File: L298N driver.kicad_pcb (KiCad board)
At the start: 2 copper layers, 75 x 75 mm, 39 parts, among them J1 Screw_Terminal_01x03, J2 Conn_01x02_Pin, J3 Conn_01x05, J4 Conn_01x05, J5 Conn_01x02, J6 Conn_01x02, J7 Conn_01x02, J8 Conn_01x02, U1 74HC595, U2 LM78M05_TO220, U3 DEV-15795, U4 L298N, U5 L298N

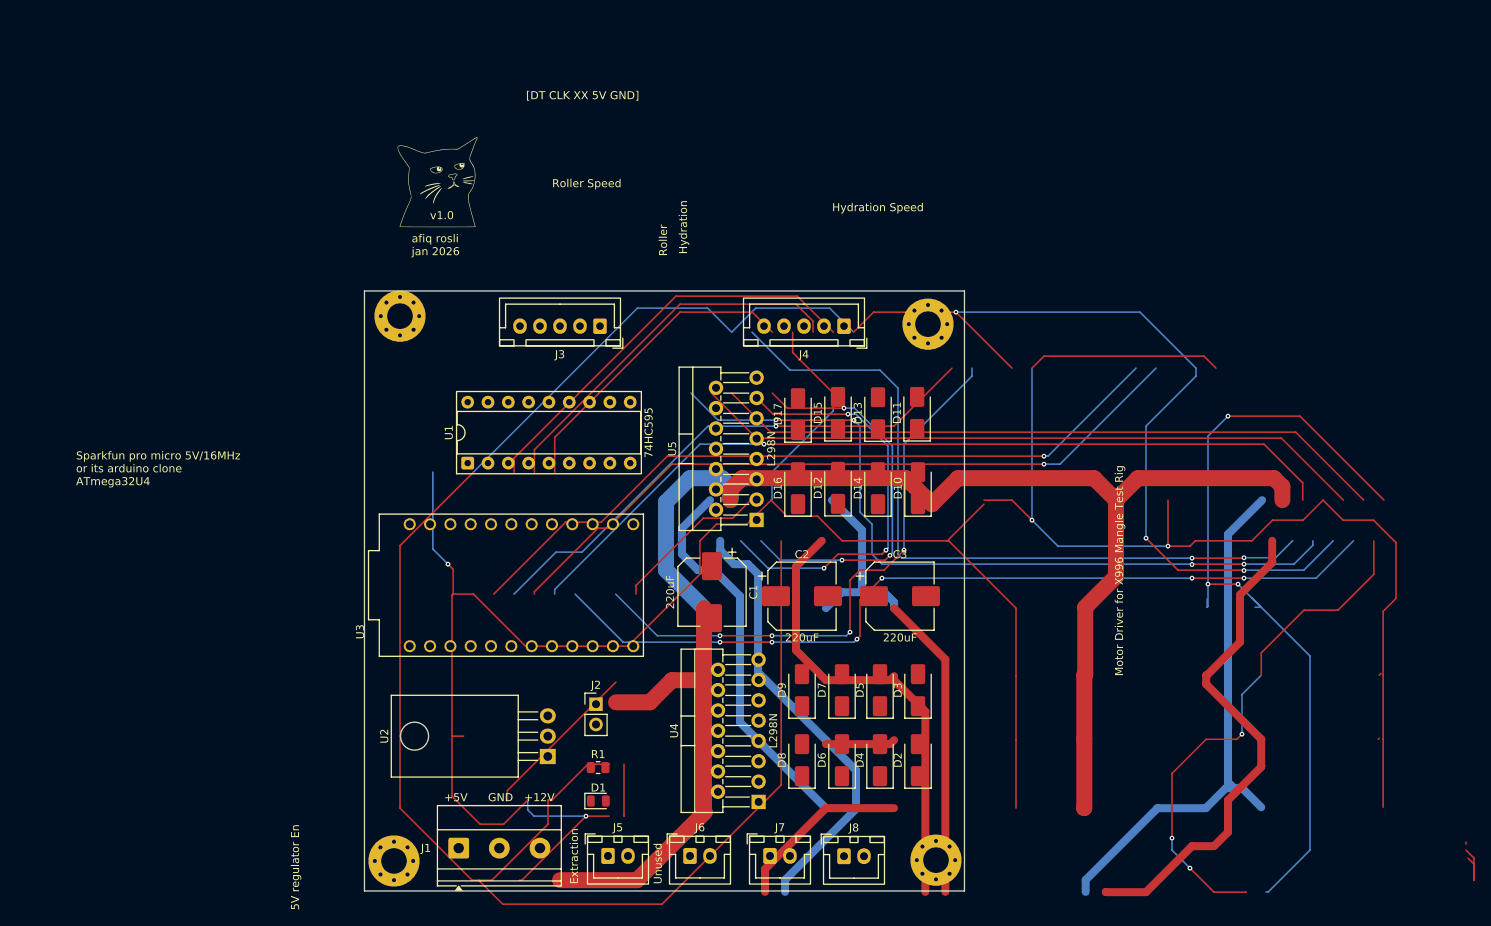
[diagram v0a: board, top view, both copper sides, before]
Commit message: draft layout for smd and 3x3 board. drc error still exist
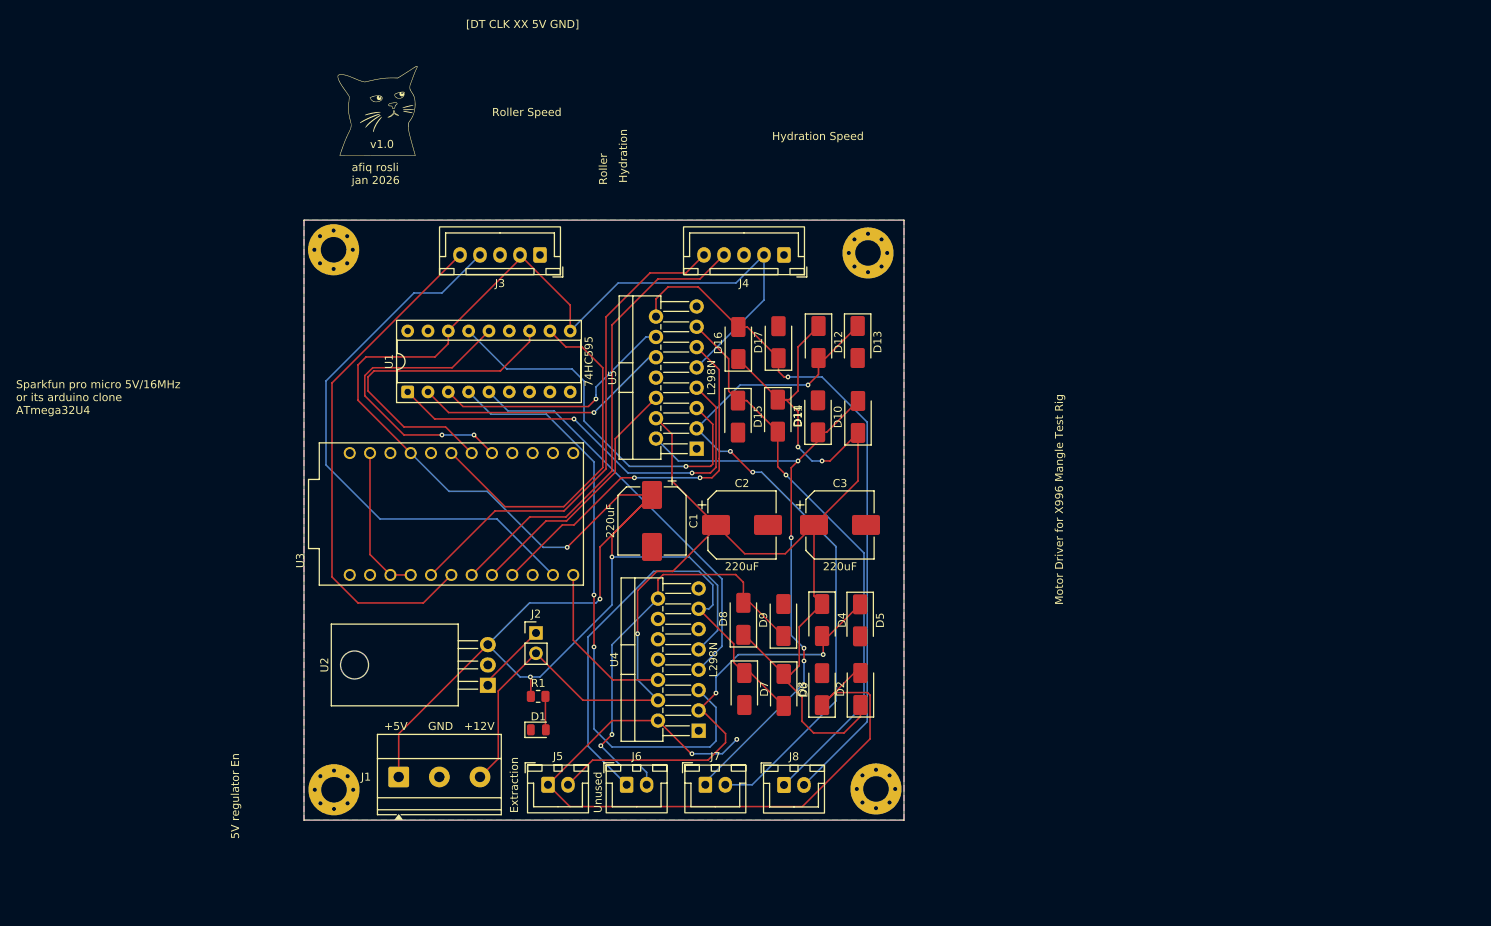
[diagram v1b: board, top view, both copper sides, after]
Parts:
- moved D16 19.6 mm to (114.3, 75.4)
- moved D8 19.1 mm to (114.9, 109.8)
- moved D4 19.0 mm to (124.8, 110.0), turned to -90 degrees
- moved D12 18.4 mm to (124.3, 75.2), turned to -90 degrees
- moved D14 15.5 mm to (119.2, 84.4), turned to -90 degrees
- moved D15 12.5 mm to (114.2, 84.6), turned to -90 degrees
- moved D11 12.4 mm to (124.2, 84.5)
- moved D7 12.2 mm to (115.0, 118.6), turned to -90 degrees
- moved J7 12.0 mm to (110.2, 130.6)
- moved D3 12.0 mm to (124.8, 118.6)
- moved J6 11.9 mm to (100.3, 130.6)
- moved H2 11.7 mm to (63.7, 63.7)
- moved C1 11.6 mm to (103.5, 97.6)
- moved C2 11.6 mm to (114.8, 98.1)
- moved C3 11.6 mm to (127.0, 98.1)
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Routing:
- net GND: track 712.9 -> 19.8 mm, vias 6 -> 0
- net VCC: track 565.9 -> 191.9 mm, vias 14 -> 3
- net Net-(D16-A): track 230.8 -> 85.8 mm, vias 3 -> 1
- net unconnected-(U3-MISO-PadJ4_10): track 105.8 -> 0.00 mm, vias 1 -> 0
- net Net-(D2-A): track 0.00 -> 93.0 mm, vias 0 -> 2
- net /rotary_enc_roller_dt: track 0.00 -> 70.3 mm
- net /rotary_enc_hydration_clk: track 131.0 -> 61.8 mm, vias 1 -> 0
- net Net-(D10-A): track 22.1 -> 76.7 mm, vias 0 -> 4
- net Net-(D6-A): track 8.73 -> 61.7 mm
- net /extraction_in2: track 0.00 -> 51.4 mm
- net /latch: track 92.3 -> 41.3 mm, vias 2 -> 0
- net /roller_in1: track 0.00 -> 48.4 mm, vias 0 -> 1
- net /hydration_En: track 0.00 -> 47.9 mm, vias 0 -> 2
- net /clk: track 0.00 -> 44.7 mm
- net /roller_in2: track 96.7 -> 54.0 mm, vias 4 -> 2
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- added copper zone on B.Cu, net GND
- added copper zone on F.Cu, net GND

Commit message: fix silkscreen and thermal relief issue
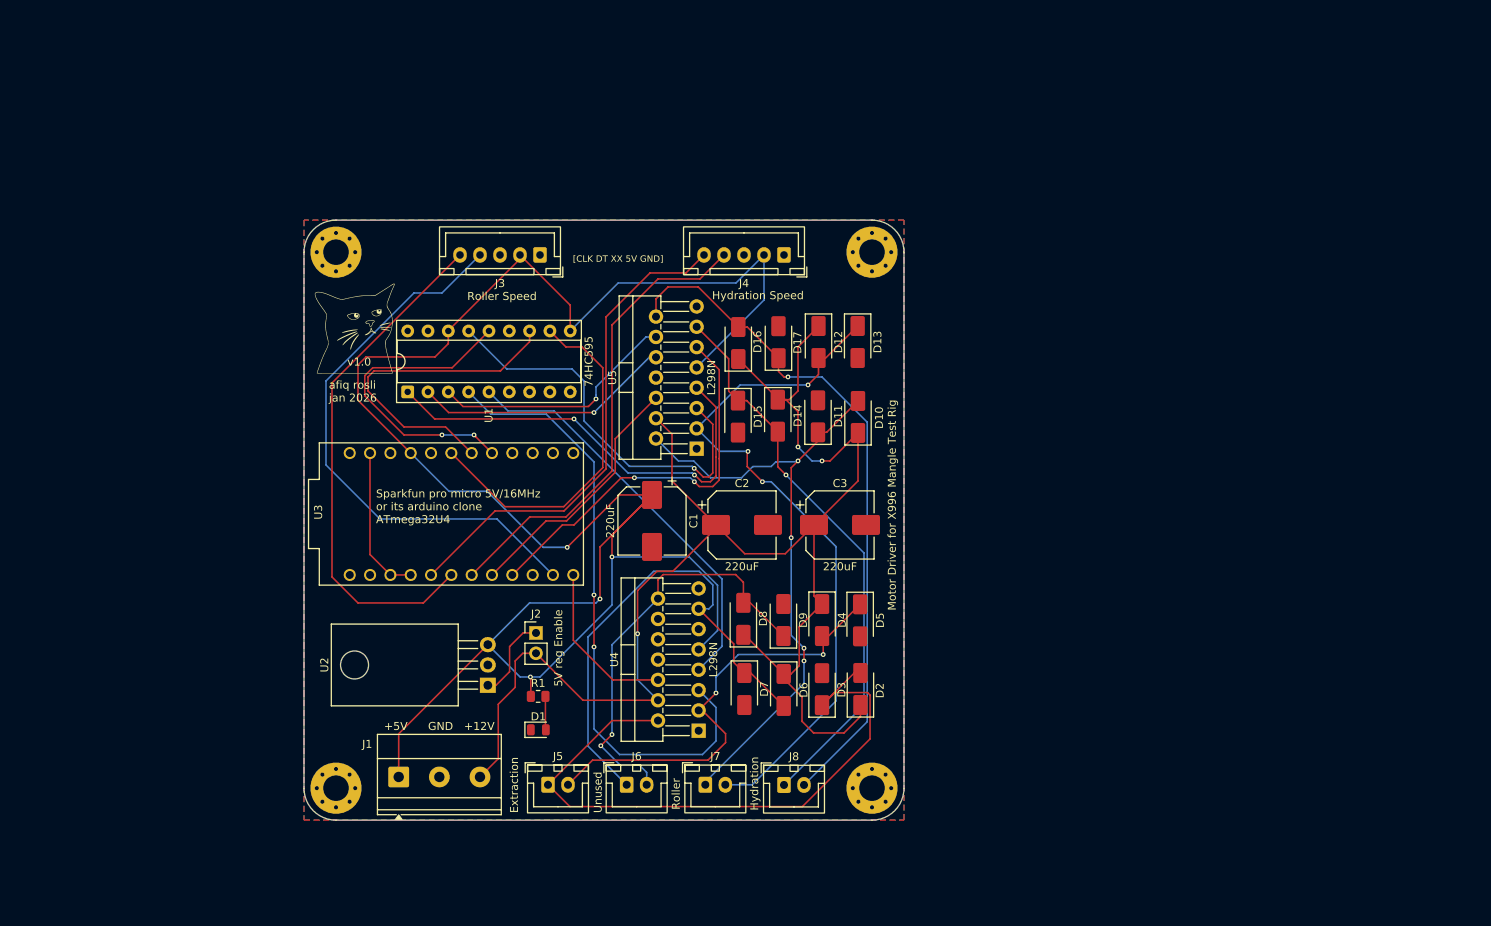
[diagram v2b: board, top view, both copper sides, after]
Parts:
- moved G*** 27.3 mm to (66.4, 73.5)
- moved H1 0.51 mm to (131.0, 64.0)
- moved H4 0.51 mm to (131.0, 131.0)
- moved H2 0.42 mm to (64.0, 64.0)
- moved H3 0.32 mm to (64.0, 131.0)
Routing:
- net Net-(D2-A): track 93.0 -> 80.7 mm, vias 2 -> 0
- net /roller_in1: track 48.4 -> 50.2 mm
- net Net-(D10-A): track 76.7 -> 78.5 mm
- net /hydration_En: track 47.9 -> 49.5 mm
- net /roller_in2: track 54.0 -> 55.5 mm
- net /power: track 9.03 -> 10.6 mm
- net Net-(D12-A): track 87.7 -> 89.0 mm
- net VCC: track 191.9 -> 192.9 mm
- net /extraction_in1: track 76.4 -> 77.2 mm
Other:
- outline, holes or cut-outs redrawn
- board text added: "5V reg Enable"
- board text added: "[CLK DT XX 5V GND]"
- board text removed: "5V regulator En"
- board text removed: "[DT CLK XX 5V GND]"

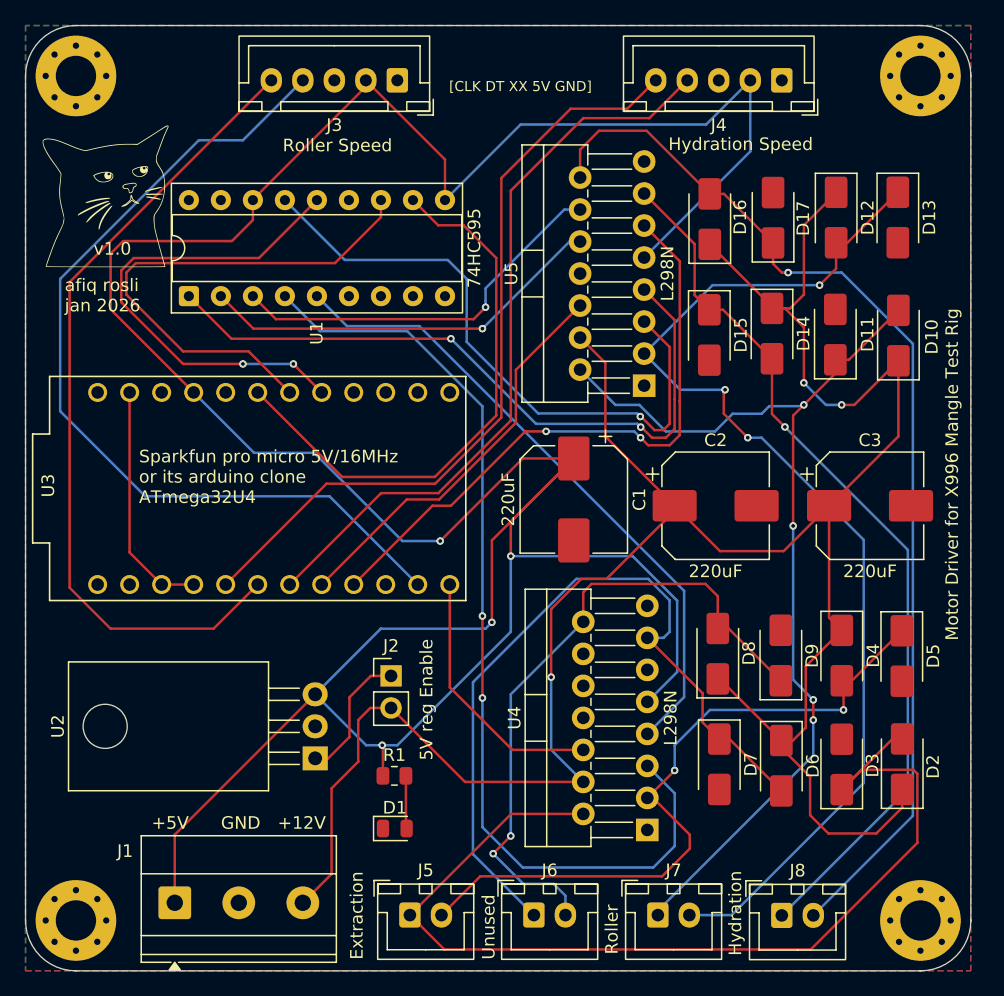
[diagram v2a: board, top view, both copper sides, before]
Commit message: update silkscreen zoning out cat
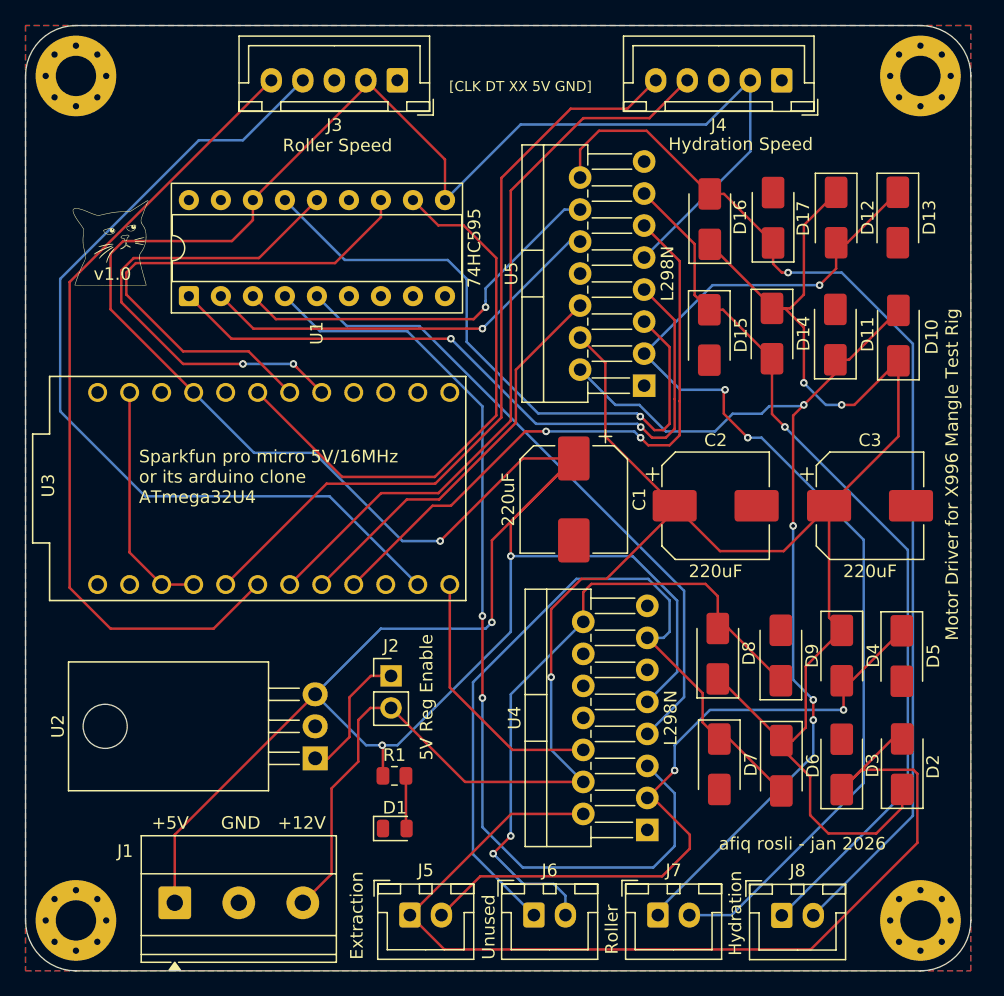
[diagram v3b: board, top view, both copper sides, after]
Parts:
- moved G*** 3.72 mm to (66.8, 77.2)
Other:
- board text added: "5V Reg Enable"
- board text added: "afiq rosli - jan 2026"
- board text removed: "5V reg Enable"
- board text removed: "afiq rosli jan 2026"

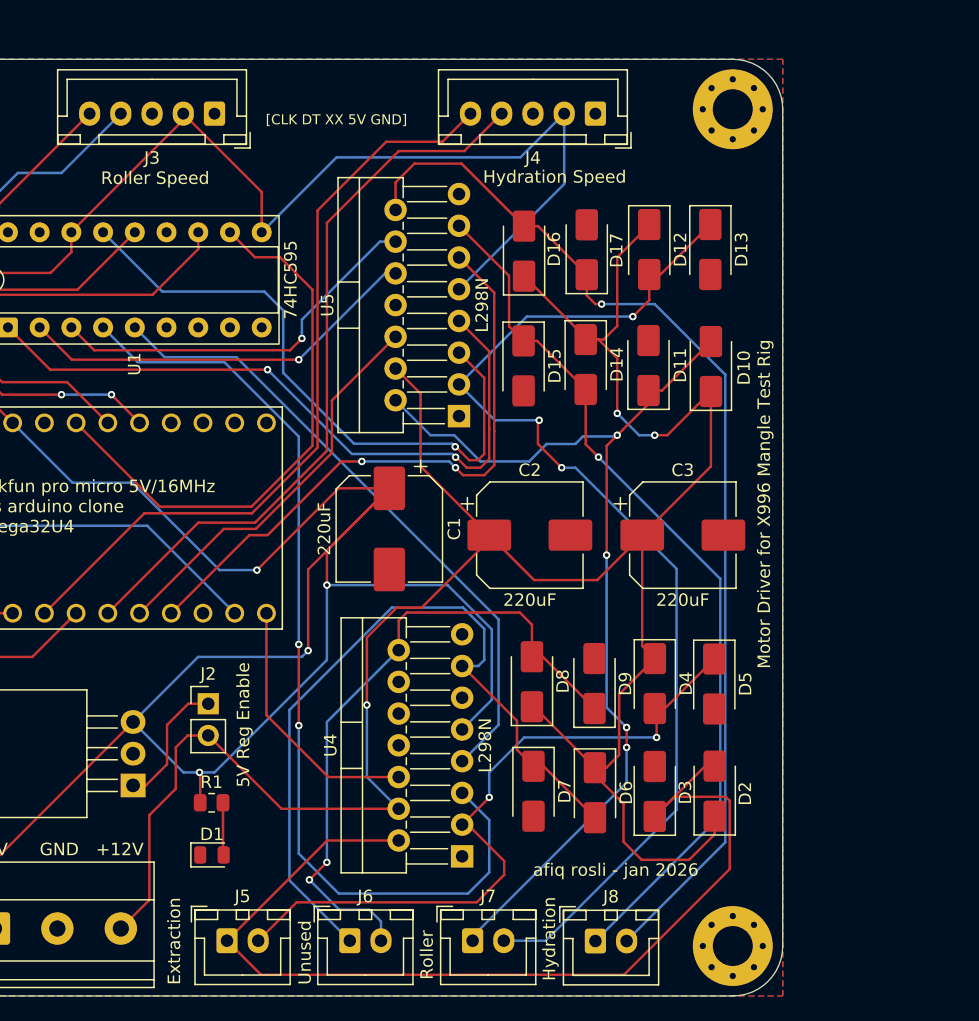
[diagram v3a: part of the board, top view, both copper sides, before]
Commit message: fat VCC traces
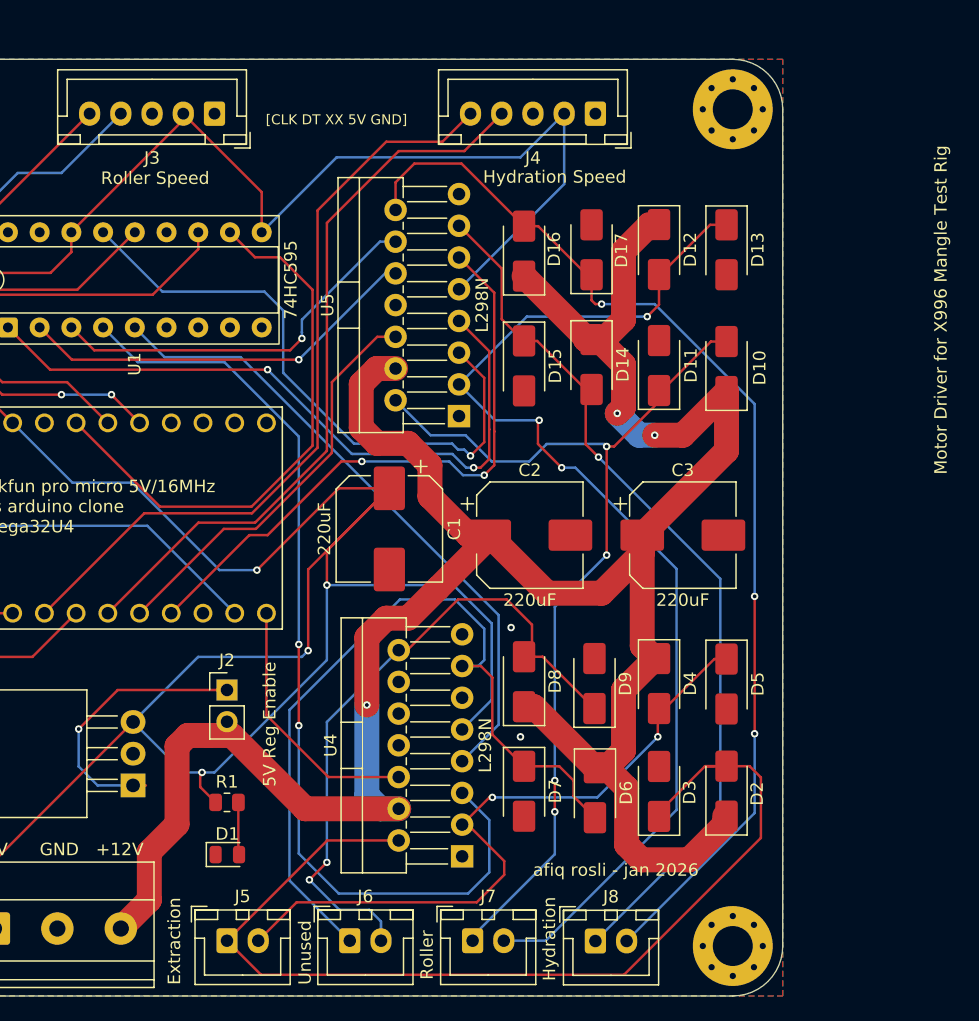
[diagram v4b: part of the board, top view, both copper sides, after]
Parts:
- moved J2 1.86 mm to (90.5, 110.5)
- moved D13 1.29 mm to (130.5, 75.2)
- moved D10 1.25 mm to (130.5, 84.6)
- moved D1 1.23 mm to (90.5, 123.7)
- moved R1 1.23 mm to (90.5, 119.5)
- moved D5 0.98 mm to (130.5, 110.0)
- moved D2 0.95 mm to (130.5, 118.6)
- moved D11 0.85 mm to (125.1, 84.5)
- moved D12 0.78 mm to (125.1, 75.2)
- moved D7 0.76 mm to (114.3, 118.6)
- moved D8 0.63 mm to (114.3, 109.8)
- moved D14 0.47 mm to (119.7, 84.4)
- moved D17 0.38 mm to (119.7, 75.2)
- moved D3 0.34 mm to (125.1, 118.6)
- moved D4 0.34 mm to (125.1, 110.0)
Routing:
- net /power: track 10.6 -> 22.2 mm, vias 0 -> 1
- net VCC: track 192.9 -> 203.0 mm
- net Net-(D6-A): track 61.7 -> 64.3 mm
- net Net-(D16-A): track 85.8 -> 87.8 mm, vias 1 -> 3
- net Net-(D12-A): track 89.0 -> 90.5 mm
- net Net-(D10-A): track 78.5 -> 77.2 mm
- net Net-(D2-A): track 80.7 -> 81.6 mm
- net /roller_En: track 32.1 -> 33.0 mm
- net /roller_in1: track 50.2 -> 49.3 mm
- net Net-(D8-A): track 53.0 -> 52.5 mm
- net GND: vias 0 -> 2
